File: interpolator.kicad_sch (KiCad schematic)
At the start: 51 parts, among them J1 Conn_02x05_Top_Bottom, SW1 SW_RCLK, SW2 SW_SG1, SW3 SW_SG0, SW4 SW_ROT, SW5 SW_SF1, SW6 SW_SF0, U1 iC-NV

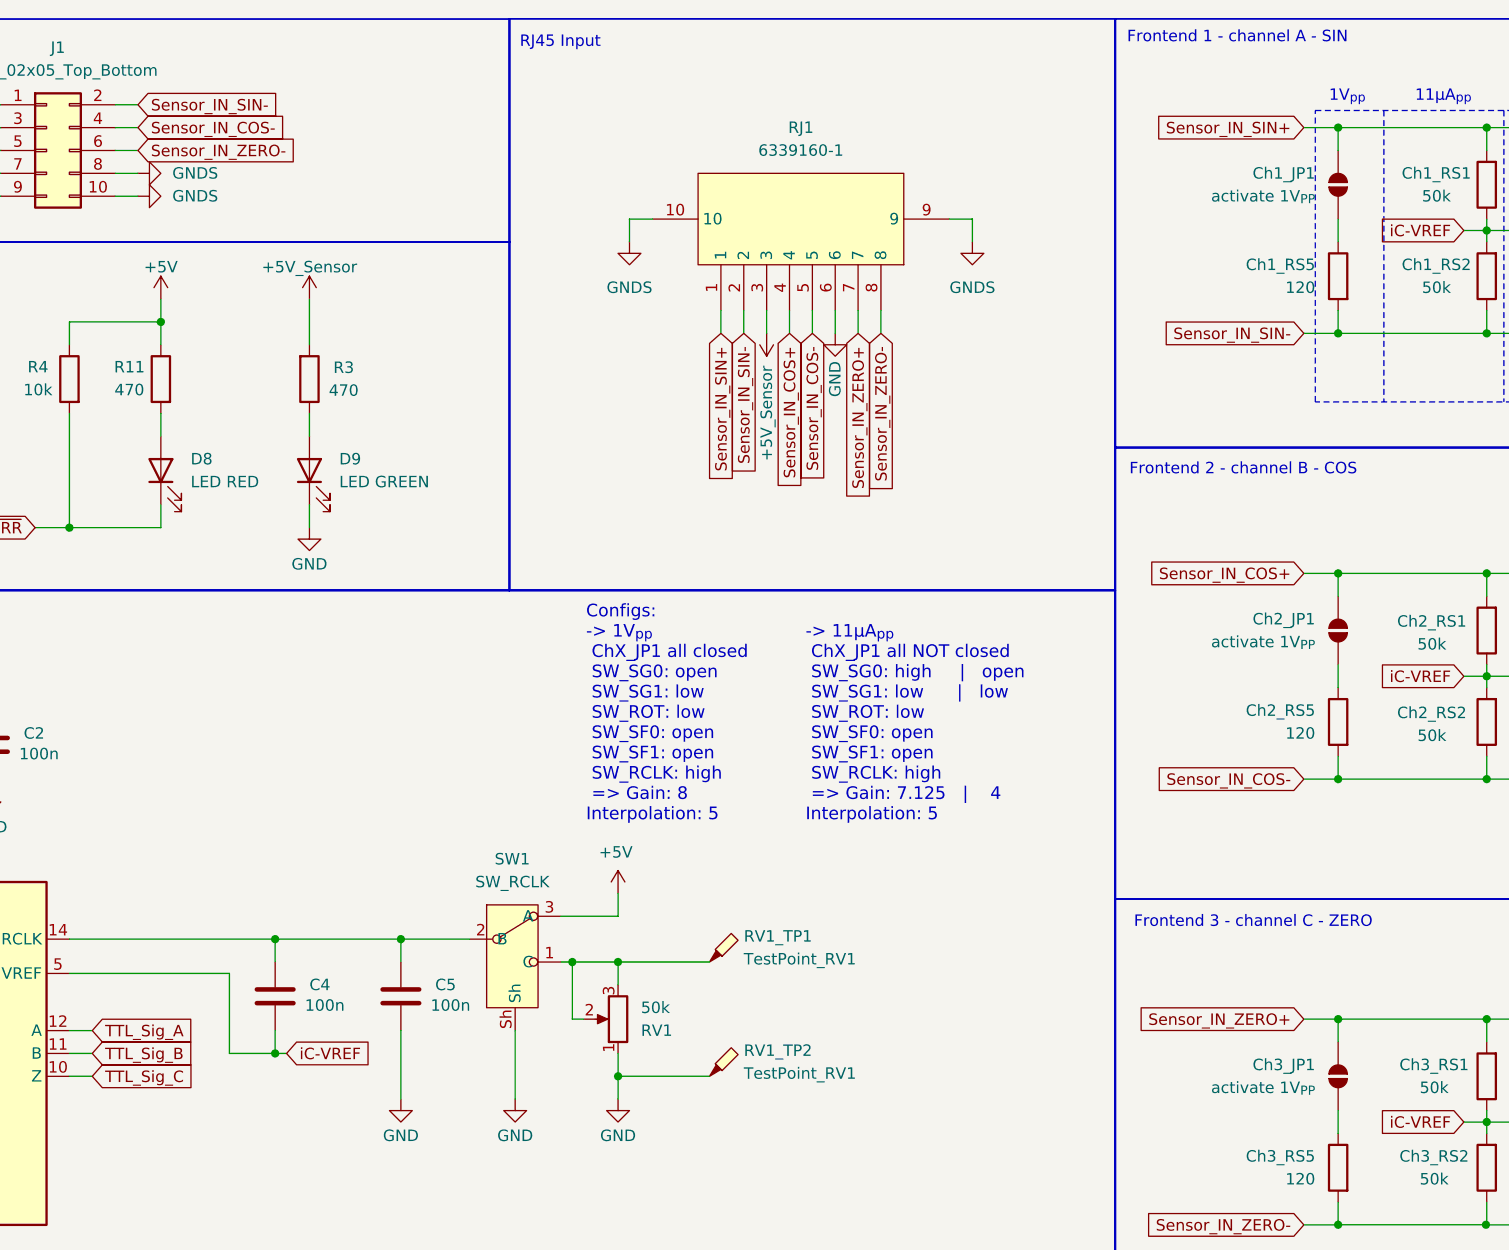
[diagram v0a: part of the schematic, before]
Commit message: Last unfinished project state -> ARCHIVED
PCB version v0.9.6 was fully working and successfully tested. Version v0.9.8 was never produced nor tested.
This board is provided as is - unfinished and untested. Productive use is explicitly not recommended! Further rework is required. No support is offered for it. The project will be left as is.
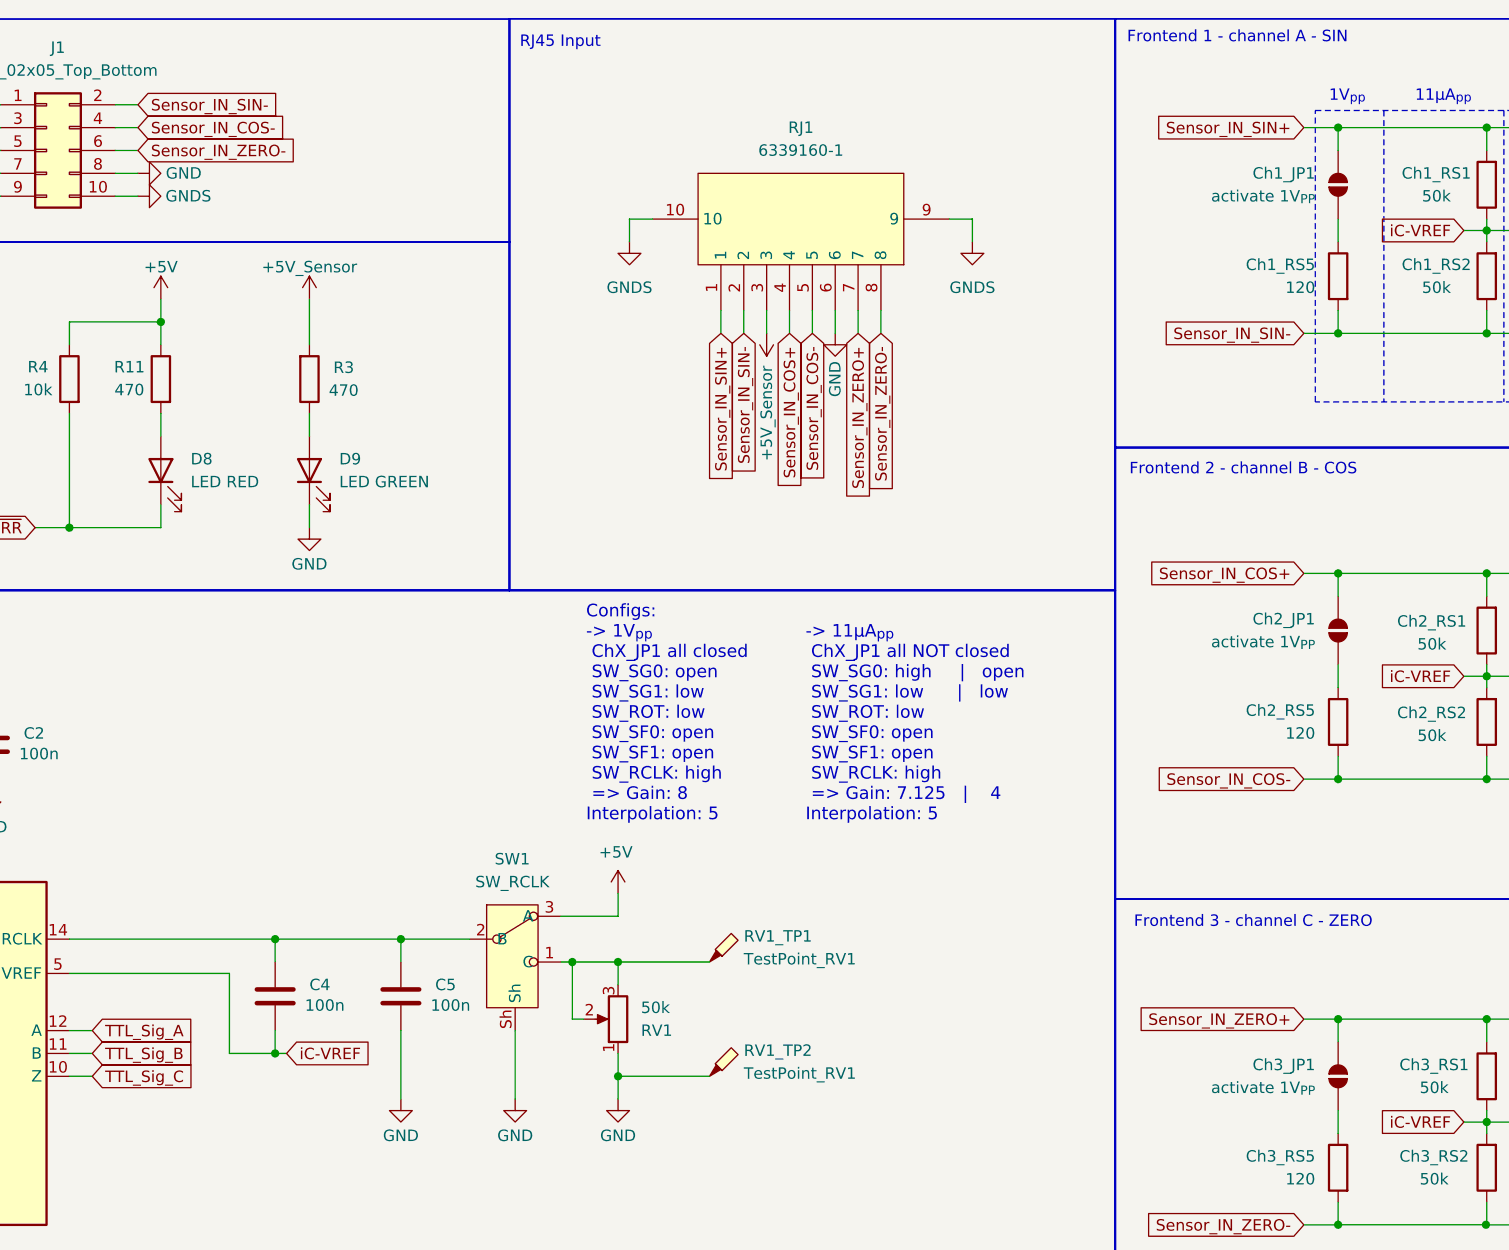
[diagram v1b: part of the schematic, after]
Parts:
- C1, C2, C4, C5: LCSC Part (none) -> C14663
- Ch1_CS1, Ch2_CS1, Ch3_CS1: LCSC Part (none) -> C107081
- Ch1_CS2, Ch2_CS2, Ch3_CS2: LCSC Part (none) -> C1622
- Ch1_CS3, Ch1_CS4, Ch2_CS3, Ch2_CS4, Ch3_CS3, Ch3_CS4: LCSC Part (none) -> C22396
- Ch1_RS5, Ch2_RS5, Ch3_RS5: LCSC Part (none) -> C22787
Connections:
- net GND: now also J1.8 (Pin_8)
- net GNDS: no longer J1.8 (Pin_8)
